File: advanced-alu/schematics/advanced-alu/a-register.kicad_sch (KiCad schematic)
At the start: 10 parts, among them U10 74LS194, U3 74LS08, U4 74LS04, U5 74LS245, U6 74LS32, U7 74LS86, U8 74LS08, U9 74LS194

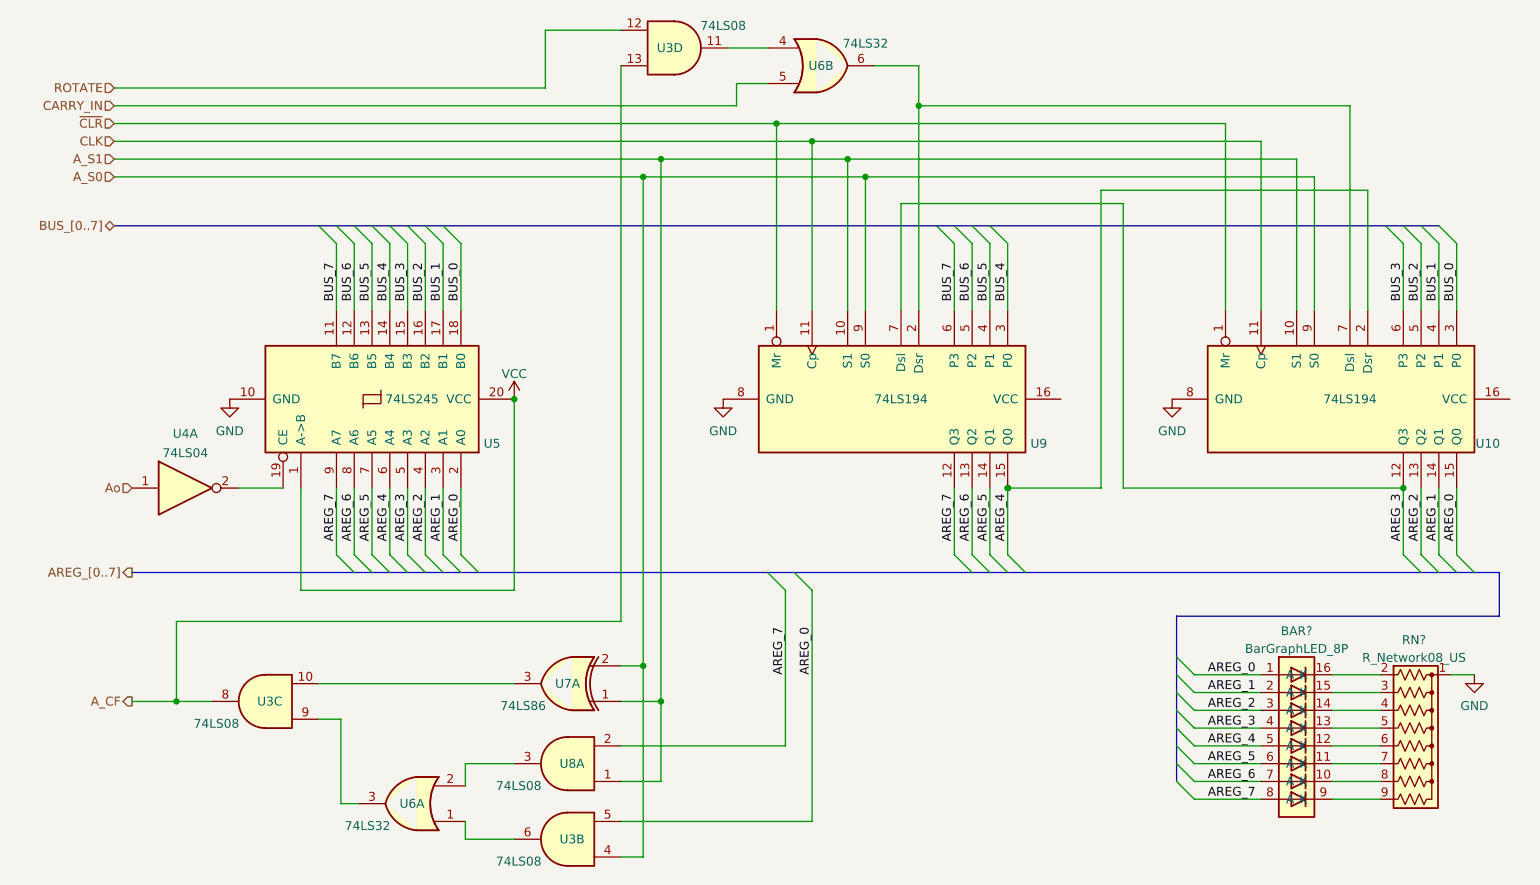
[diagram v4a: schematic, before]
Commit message: updated design to properly handle subtractions
Also added ability to do an arithmetic right shift.
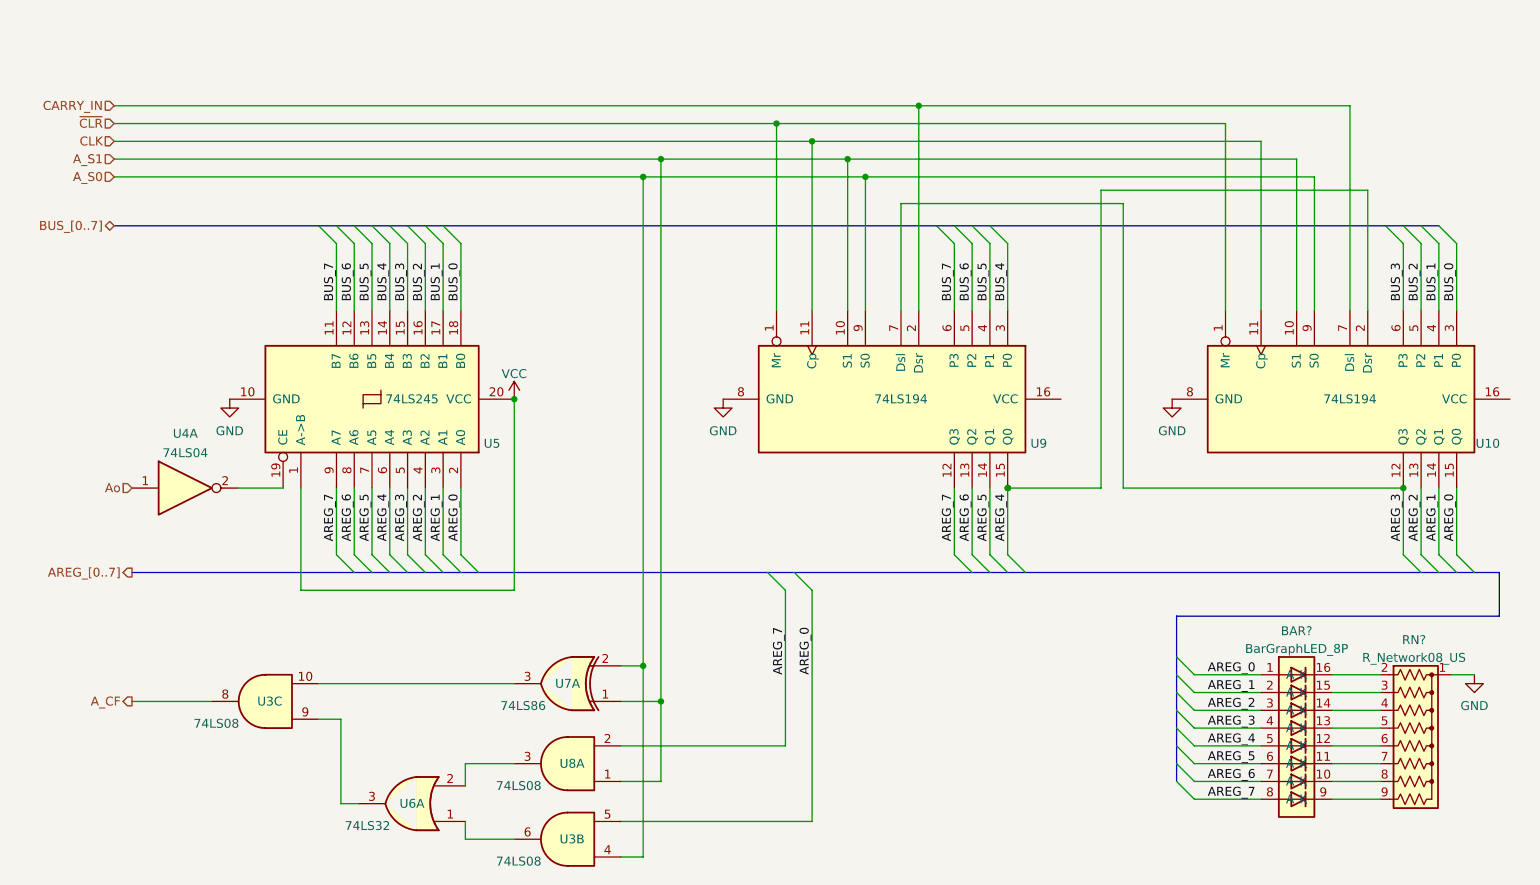
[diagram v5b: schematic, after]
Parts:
- removed unit 4 of U3
- removed unit 2 of U6
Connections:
- net CARRY_IN: now also U10.7 (Dsl), U9.2 (Dsr)
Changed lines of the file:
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@@
   (junction (at 179.705 106.68) (diameter 0) (color 0 0 0 0)
   )
+  (junction (at 159.385 62.23) (diameter 0) (color 0 0 0 0)
+  )
+  (junction (at 127.635 132.08) (diameter 0) (color 0 0 0 0)
+  )
+  (junction (at 151.765 57.15) (diameter 0) (color 0 0 0 0)
+  )
+  (junction (at 127.635 62.23) (diameter 0) (color 0 0 0 0)
+  )
+  (junction (at 109.22 93.98) (diameter 0) (color 0 0 0 0)
+  )
   (junction (at 167.005 52.07) (diameter 0) (color 0 0 0 0)
   )
-  (junction (at 60.96 137.16) (diameter 0) (color 0 0 0 0)
-  )
-  (junction (at 159.385 62.23) (diameter 0) (color 0 0 0 0)
-  )
-  (junction (at 127.635 132.08) (diameter 0) (color 0 0 0 0)
-  )
-  (junction (at 151.765 57.15) (diameter 0) (color 0 0 0 0)
-  )
-  (junction (at 127.635 62.23) (diameter 0) (color 0 0 0 0)
-  )
-  (junction (at 109.22 93.98) (diameter 0) (color 0 0 0 0)
-  )
   (junction (at 236.22 106.68) (diameter 0) (color 0 0 0 0)
   )
@@
     (stroke (width 0) (type default) (color 0 0 0 0))
   )
-  (wire (pts (xy 167.005 46.355) (xy 167.005 52.07))
-    (stroke (width 0) (type default) (color 0 0 0 0))
-  )
   (bus (pts (xy 236.22 69.215) (xy 238.76 69.215))
     (stroke (width 0) (type default) (color 0 0 0 0))
@@
     (stroke (width 0) (type default) (color 0 0 0 0))
   )
-  (wire (pts (xy 54.61 137.16) (xy 60.96 137.16))
-    (stroke (width 0) (type default) (color 0 0 0 0))
-  )
   (wire (pts (xy 164.465 66.04) (xy 164.465 81.28))
     (stroke (width 0) (type default) (color 0 0 0 0))
@@
     (stroke (width 0) (type default) (color 0 0 0 0))
   )
-  (wire (pts (xy 139.7 43.815) (xy 145.415 43.815))
-    (stroke (width 0) (type default) (color 0 0 0 0))
-  )
   (wire (pts (xy 86.36 106.68) (xy 86.36 116.205))
     (stroke (width 0) (type default) (color 0 0 0 0))
@@
     (stroke (width 0) (type default) (color 0 0 0 0))
   )
-  (wire (pts (xy 140.97 52.07) (xy 140.97 48.895))
-    (stroke (width 0) (type default) (color 0 0 0 0))
-  )
   (wire (pts (xy 226.06 146.05) (xy 232.918 146.05))
     (stroke (width 0) (type default) (color 0 0 0 0))
@@
     (stroke (width 0) (type default) (color 0 0 0 0))
   )
-  (wire (pts (xy 124.46 46.355) (xy 124.46 125.73))
-    (stroke (width 0) (type default) (color 0 0 0 0))
-  )
   (wire (pts (xy 215.9 148.59) (xy 206.375 148.59))
     (stroke (width 0) (type default) (color 0 0 0 0))
@@
     (stroke (width 0) (type default) (color 0 0 0 0))
   )
-  (wire (pts (xy 60.96 137.16) (xy 60.96 125.73))
-    (stroke (width 0) (type default) (color 0 0 0 0))
-  )
   (wire (pts (xy 238.76 71.755) (xy 238.76 81.28))
     (stroke (width 0) (type default) (color 0 0 0 0))
@@
     (stroke (width 0) (type default) (color 0 0 0 0))
   )
-  (wire (pts (xy 140.97 48.895) (xy 145.415 48.895))
-    (stroke (width 0) (type default) (color 0 0 0 0))
-  )
   (bus (pts (xy 96.52 118.745) (xy 99.06 118.745))
     (stroke (width 0) (type default) (color 0 0 0 0))
@@
     (stroke (width 0) (type default) (color 0 0 0 0))
   )
-  (wire (pts (xy 60.96 137.16) (xy 66.04 137.16))
+  (wire (pts (xy 54.61 137.16) (xy 66.04 137.16))
     (stroke (width 0) (type default) (color 0 0 0 0))
   )
@@
     (stroke (width 0) (type default) (color 0 0 0 0))
   )
-  (wire (pts (xy 52.07 49.53) (xy 113.665 49.53))
-    (stroke (width 0) (type default) (color 0 0 0 0))
-  )
   (wire (pts (xy 96.52 106.68) (xy 96.52 116.205))
     (stroke (width 0) (type default) (color 0 0 0 0))
@@
     (stroke (width 0) (type default) (color 0 0 0 0))
   )
-  (wire (pts (xy 160.655 46.355) (xy 167.005 46.355))
-    (stroke (width 0) (type default) (color 0 0 0 0))
-  )
   (wire (pts (xy 91.44 71.755) (xy 91.44 81.28))
     (stroke (width 0) (type default) (color 0 0 0 0))
   )
+  (wire (pts (xy 52.07 52.07) (xy 167.005 52.07))
+    (stroke (width 0) (type default) (color 0 0 0 0))
+  )
   (wire (pts (xy 174.625 106.68) (xy 174.625 116.205))
     (stroke (width 0) (type default) (color 0 0 0 0))
@@
     (stroke (width 0) (type default) (color 0 0 0 0))
   )
-  (wire (pts (xy 52.07 52.07) (xy 140.97 52.07))
-    (stroke (width 0) (type default) (color 0 0 0 0))
-  )
   (wire (pts (xy 196.215 106.68) (xy 196.215 66.04))
     (stroke (width 0) (type default) (color 0 0 0 0))
@@
     (stroke (width 0) (type default) (color 0 0 0 0))
   )
-  (wire (pts (xy 60.96 125.73) (xy 124.46 125.73))
-    (stroke (width 0) (type default) (color 0 0 0 0))
-  )
   (wire (pts (xy 52.07 57.15) (xy 151.765 57.15))
     (stroke (width 0) (type default) (color 0 0 0 0))
@@
     (stroke (width 0) (type default) (color 0 0 0 0))
   )
-  (wire (pts (xy 113.665 41.275) (xy 124.46 41.275))
-    (stroke (width 0) (type default) (color 0 0 0 0))
-  )
   (wire (pts (xy 127.635 62.23) (xy 127.635 132.08))
     (stroke (width 0) (type default) (color 0 0 0 0))
@@
   )
   (bus (pts (xy 249.936 118.745) (xy 249.936 124.968))
-    (stroke (width 0) (type default) (color 0 0 0 0))
-  )
-  (wire (pts (xy 113.665 49.53) (xy 113.665 41.275))
     (stroke (width 0) (type default) (color 0 0 0 0))
   )
@@
   )
   (hierarchical_label "BUS_[0..7]" (shape bidirectional) (at 52.07 69.215 180)
-    (effects (font (size 1.27 1.27)) (justify right))
-  )
-  (hierarchical_label "ROTATE" (shape input) (at 52.07 49.53 180)
     (effects (font (size 1.27 1.27)) (justify right))
   )
@@
     (pin "2")
     (pin "3")
-  )
-  (symbol (lib_id "74xx:74LS32") (at 153.035 46.355 0) (unit 2)
-    (in_bom yes) (on_board yes)
-    (property "Reference" "U6" (id 0) (at 153.035 46.355 0))
-    (property "Value" "74LS32" (id 1) (at 159.385 43.18 0))
-    (property "Footprint" "" (id 2) (at 153.035 46.355 0)
-      (effects (font (size 1.27 1.27)) hide)
-    )
-    (property "Datasheet" "http://www.ti.com/lit/gpn/sn74LS32" (id 3) (at 153.035 46.355 0)
-      (effects (font (size 1.27 1.27)) hide)
-    )
-    (pin "4")
-    (pin "5")
-    (pin "6")
   )
   (symbol (lib_id "power:VCC") (at 109.22 93.98 0) (unit 1)
@@
     (pin "1")
   )
-  (symbol (lib_id "74xx:74LS08") (at 132.08 43.815 0) (unit 4)
-    (in_bom yes) (on_board yes)
-    (property "Reference" "U3" (id 0) (at 131.445 43.815 0))
-    (property "Value" "74LS08" (id 1) (at 139.065 40.64 0))
-    (property "Footprint" "" (id 2) (at 132.08 43.815 0)
-      (effects (font (size 1.27 1.27)) hide)
-    )
-    (property "Datasheet" "http://www.ti.com/lit/gpn/sn74LS08" (id 3) (at 132.08 43.815 0)
-      (effects (font (size 1.27 1.27)) hide)
-    )
-    (pin "11")
-    (pin "12")
-    (pin "13")
-  )
   (symbol (lib_id "74xx:74LS194") (at 164.465 93.98 270) (unit 1)

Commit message: tweaks and layout improvements
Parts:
- gave numbers to parts that had none: 2
- renumbered U4 to U3, U3 to U4
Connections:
- net A_CF: now also U4.11; no longer U4.8
- net VCC: now also U10.16 (VCC), U9.16 (VCC)
- net at U7.3: now also U4.13; no longer U4.10
- net at U6.3: now also U4.12; no longer U4.9
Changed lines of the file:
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@@
   (symbol (lib_id "common-symbols:BarGraphLED_8P") (at 220.98 143.51 0) (unit 1)
     (in_bom yes) (on_board yes) (fields_autoplaced)
-    (property "Reference" "BAR?" (id 0) (at 220.98 127.1102 0))
+    (property "Reference" "BAR1" (id 0) (at 220.98 127.1102 0))
     (property "Value" "BarGraphLED_8P" (id 1) (at 220.98 129.6471 0))
     (property "Footprint" "" (id 2) (at 220.98 143.51 0)
@@
     (pin "2")
     (pin "3")
-    (pin "4")
-    (pin "5")
-    (pin "6")
-    (pin "10")
-    (pin "8")
-    (pin "9")
-    (pin "11")
-    (pin "12")
-    (pin "13")
-    (pin "14")
-    (pin "7")
   )
   (symbol (lib_id "power:VCC") (at 109.22 93.98 0) (unit 1)
@@
   (symbol (lib_id "Device:R_Network08_US") (at 237.998 143.51 270) (unit 1)
     (in_bom yes) (on_board yes) (fields_autoplaced)
-    (property "Reference" "RN?" (id 0) (at 237.744 128.3802 90))
+    (property "Reference" "RN1" (id 0) (at 237.744 128.3802 90))
     (property "Value" "R_Network08_US" (id 1) (at 237.744 130.9171 90))
     (property "Footprint" "Resistor_THT:R_Array_SIP9" (id 2) (at 237.998 155.575 90)
@@
     )
     (property "Datasheet" "" (id 3) (at 139.065 93.98 0)
+      (effects (font (size 1.27 1.27)) hide)
+    )
+    (pin "1")
+  )
+  (symbol (lib_id "power:VCC") (at 251.46 93.98 0) (unit 1)
+    (in_bom yes) (on_board yes) (fields_autoplaced)
+    (property "Reference" "#PWR09" (id 0) (at 251.46 97.79 0)
+      (effects (font (size 1.27 1.27)) hide)
+    )
+    (property "Value" "VCC" (id 1) (at 251.46 90.3755 0))
+    (property "Footprint" "" (id 2) (at 251.46 93.98 0)
+      (effects (font (size 1.27 1.27)) hide)
+    )
+    (property "Datasheet" "" (id 3) (at 251.46 93.98 0)
+      (effects (font (size 1.27 1.27)) hide)
+    )
+    (pin "1")
+  )
+  (symbol (lib_id "power:VCC") (at 187.325 93.98 0) (unit 1)
+    (in_bom yes) (on_board yes) (fields_autoplaced)
+    (property "Reference" "#PWR06" (id 0) (at 187.325 97.79 0)
+      (effects (font (size 1.27 1.27)) hide)
+    )
+    (property "Value" "VCC" (id 1) (at 187.325 90.3755 0))
+    (property "Footprint" "" (id 2) (at 187.325 93.98 0)
+      (effects (font (size 1.27 1.27)) hide)
+    )
+    (property "Datasheet" "" (id 3) (at 187.325 93.98 0)
       (effects (font (size 1.27 1.27)) hide)
     )
@@
   (symbol (lib_id "74xx:74LS04") (at 62.23 106.68 0) (unit 1)
     (in_bom yes) (on_board yes) (fields_autoplaced)
-    (property "Reference" "U4" (id 0) (at 62.23 98.9035 0))
+    (property "Reference" "U3" (id 0) (at 62.23 98.9035 0))
     (property "Value" "74LS04" (id 1) (at 62.23 101.6786 0))
     (property "Footprint" "" (id 2) (at 62.23 106.68 0)
@@
     (pin "1")
     (pin "2")
-    (pin "3")
-    (pin "4")
-    (pin "5")
-    (pin "6")
-    (pin "8")
-    (pin "9")
-    (pin "10")
-    (pin "11")
-    (pin "12")
-    (pin "13")
-    (pin "14")
-    (pin "7")
   )
   (symbol (lib_id "power:GND") (at 68.58 93.98 0) (unit 1)
@@
     (pin "2")
     (pin "3")
-    (pin "4")
-    (pin "5")
-    (pin "6")
-    (pin "10")
-    (pin "8")
-    (pin "9")
-    (pin "11")
-    (pin "12")
-    (pin "13")
-    (pin "14")
-    (pin "7")
   )
   (symbol (lib_id "74xx:74LS08") (at 116.84 156.845 180) (unit 2)
     (in_bom yes) (on_board yes)
-    (property "Reference" "U3" (id 0) (at 117.475 156.845 0))
+    (property "Reference" "U4" (id 0) (at 117.475 156.845 0))
     (property "Value" "74LS08" (id 1) (at 109.855 160.02 0))
     (property "Footprint" "" (id 2) (at 116.84 156.845 0)
@@
       (effects (font (size 1.27 1.27)) hide)
     )
-    (pin "1")
-    (pin "2")
-    (pin "3")
-    (pin "4")
-    (pin "5")
-    (pin "6")
-    (pin "10")
-    (pin "8")
-    (pin "9")
-    (pin "11")
-    (pin "12")
-    (pin "13")
-    (pin "14")
-    (pin "7")
+    (pin "4")
+    (pin "5")
+    (pin "6")
   )
   (symbol (lib_id "power:GND") (at 246.38 133.35 0) (unit 1)
     (in_bom yes) (on_board yes) (fields_autoplaced)
-    (property "Reference" "#PWR?" (id 0) (at 246.38 139.7 0)
+    (property "Reference" "#PWR08" (id 0) (at 246.38 139.7 0)
       (effects (font (size 1.27 1.27)) hide)
     )
@@
     (pin "1")
   )
-  (symbol (lib_id "74xx:74LS08") (at 73.66 137.16 180) (unit 3)
-    (in_bom yes) (on_board yes)
-    (property "Reference" "U3" (id 0) (at 74.295 137.16 0))
+  (symbol (lib_id "74xx:74LS08") (at 73.66 137.16 180) (unit 4)
+    (in_bom yes) (on_board yes)
+    (property "Reference" "U4" (id 0) (at 74.295 137.16 0))
     (property "Value" "74LS08" (id 1) (at 66.675 140.335 0))
     (property "Footprint" "" (id 2) (at 73.66 137.16 0)
@@
       (effects (font (size 1.27 1.27)) hide)
     )
-    (pin "1")
-    (pin "2")
-    (pin "3")
-    (pin "4")
-    (pin "5")
-    (pin "6")
-    (pin "10")
-    (pin "8")
-    (pin "9")
-    (pin "11")
-    (pin "12")
-    (pin "13")
-    (pin "14")
-    (pin "7")
+    (pin "11")
+    (pin "12")
+    (pin "13")
   )
   (symbol (lib_id "power:GND") (at 203.2 93.98 0) (unit 1)
     (in_bom yes) (on_board yes) (fields_autoplaced)
-    (property "Reference" "#PWR06" (id 0) (at 203.2 100.33 0)
+    (property "Reference" "#PWR07" (id 0) (at 203.2 100.33 0)
       (effects (font (size 1.27 1.27)) hide)
     )
@@
     (pin "2")
     (pin "3")
-    (pin "4")
-    (pin "5")
-    (pin "6")
-    (pin "10")
-    (pin "8")
-    (pin "9")
-    (pin "11")
-    (pin "12")
-    (pin "13")
-    (pin "14")
-    (pin "7")
   )
 )
